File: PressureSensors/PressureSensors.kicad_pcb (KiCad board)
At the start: 2 copper layers, 40 x 40 mm, 32 parts, among them J1 Conn_02x03_Odd_Even, U1 LPS22HB, U2 LPS22HB, U3 LPS22HB, U4 LPS22HB, U5 PCA9548ADB, U6 K78xxJT-500R3

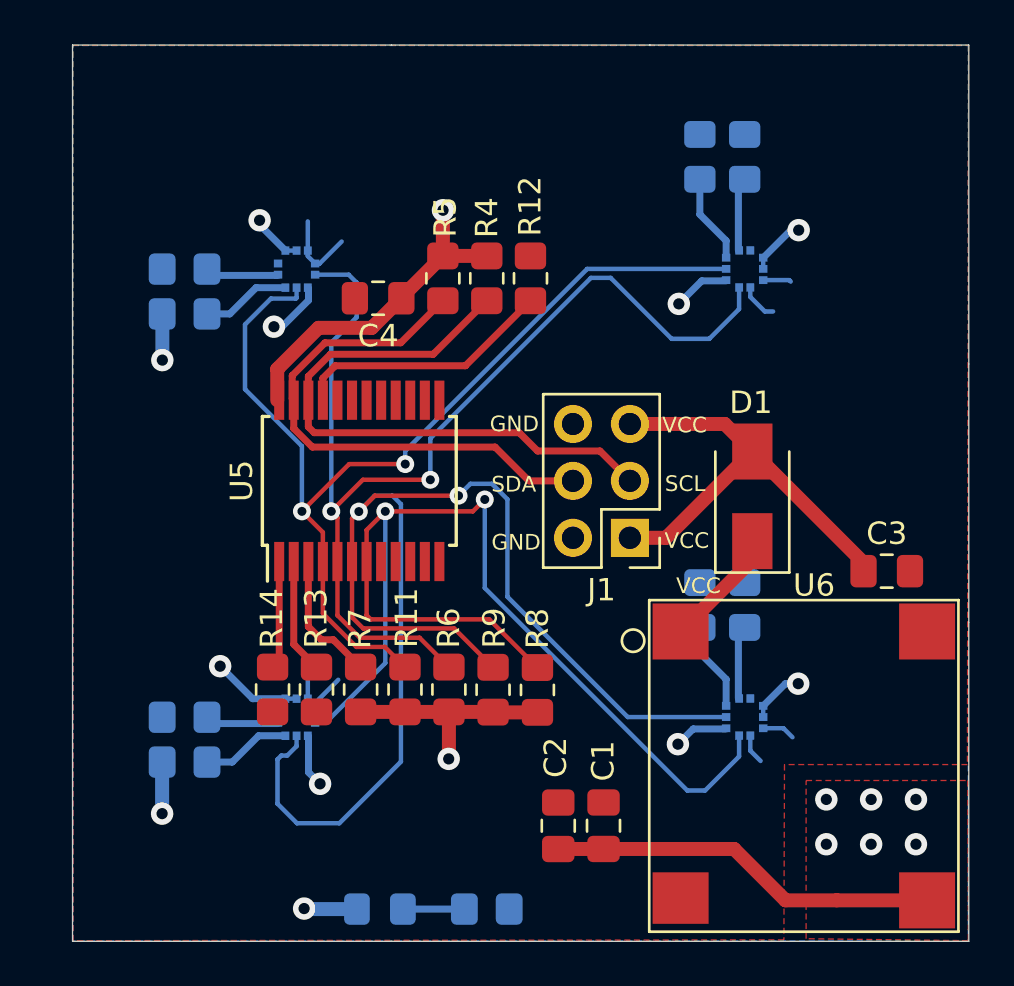
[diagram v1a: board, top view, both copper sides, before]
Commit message: Changed I2C multiplexer to 2 channel
Changed power source to LDO

Corrected spacing between sensors

Added missing capacitor for sensors

Eliminated unnecesary resistors for sensors
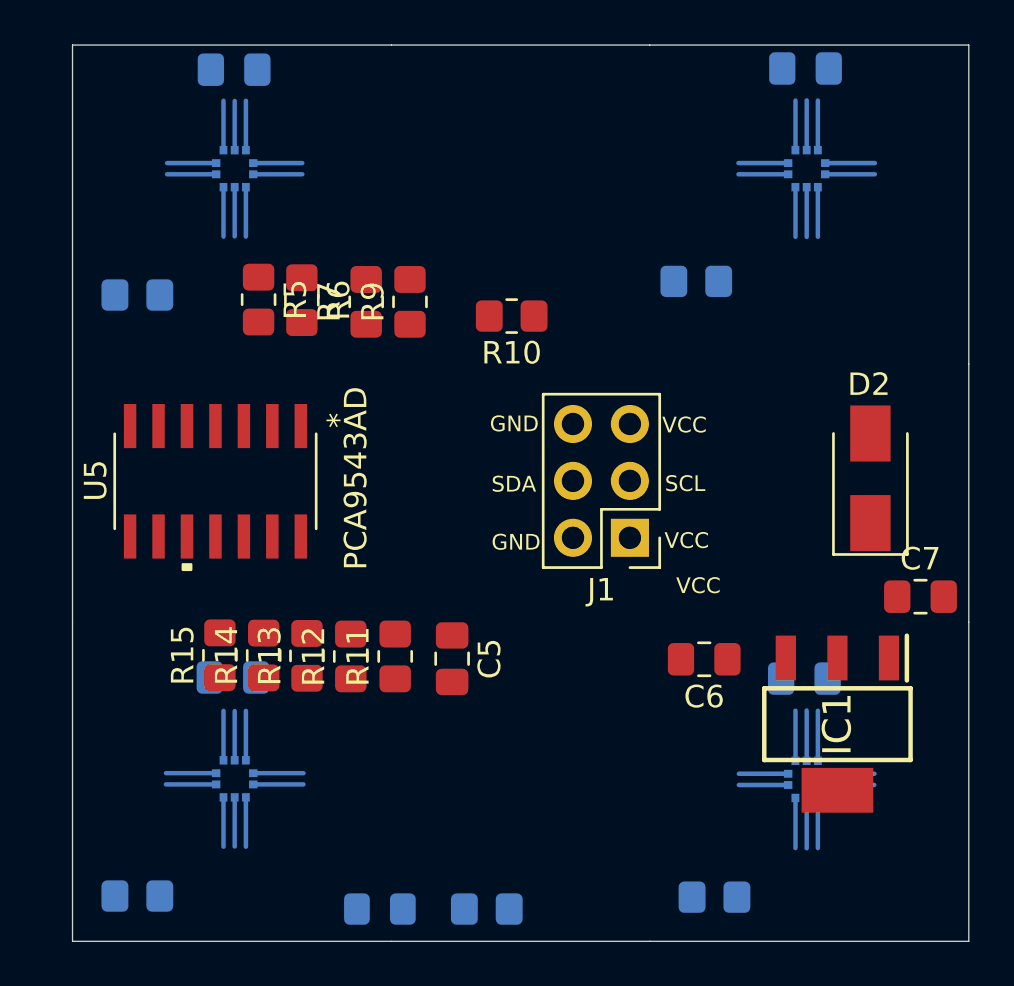
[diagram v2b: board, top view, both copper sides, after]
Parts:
- removed the R1 at (153.8, 62.8)
- removed R16, R17: 10k, Resistor_SMD:R_0805_2012Metric_Pad1.20x1.40mm_HandSolder
- removed the R4 at (142.3, 68.2)
- removed the R8 at (144.6, 86.6)
- removed U6: K78xxJT-500R3, Custom:K7803JT-500R3-SMD
- added C5: 1u, Capacitor_SMD:C_0805_2012Metric_Pad1.18x1.45mm_HandSolder, F.Cu at (140.8, 85.2)
- added C6: 4.7u, Capacitor_SMD:C_0805_2012Metric_Pad1.18x1.45mm_HandSolder, F.Cu at (152.0, 85.2)
- added C7: 0.1u, Capacitor_SMD:C_0805_2012Metric_Pad1.18x1.45mm_HandSolder, F.Cu at (161.7, 82.4)
- added IC1: BD733L2FP3-CE2, Custom:SOT230P700X180-4N, F.Cu at (158.0, 88.1)
- added R10: 10k, Resistor_SMD:R_0805_2012Metric_Pad1.20x1.40mm_HandSolder, F.Cu at (143.4, 69.9)
- C1, C2: value 22u -> 100n; moved to B.Cu
- C3: value 10u -> 100n; moved to B.Cu
- C4: value 1u -> 100n; moved to B.Cu
- R15: moved to F.Cu
- U5: value PCA9548ADB -> PCA9543AD; footprint Package_SO:SSOP-24_5.3x8.2mm_P0.65mm -> Custom:PCA9543AD
- moved C2 36.7 mm to (131.1, 58.9), turned to 180 degrees
- moved C1 35.0 mm to (156.6, 58.8), turned to 180 degrees
- moved R12 18.7 mm to (136.3, 85.1), turned to 90 degrees
- moved R6 18.6 mm to (134.1, 69.2), turned to -90 degrees
- moved C4 18.1 mm to (131.0, 86.0)
- moved R9 17.7 mm to (138.9, 69.2)
- moved R7 17.4 mm to (137.0, 69.2)
- moved R15 17.3 mm to (130.4, 85.0), turned to 90 degrees
- moved R2 13.1 mm to (152.5, 95.8), turned to 0 degrees
- moved R5 8.28 mm to (132.2, 69.1)
- moved U5 6.42 mm to (130.2, 77.2), turned to -90 degrees
- moved R4 6.34 mm to (126.7, 95.8)
- moved C3 6.04 mm to (156.5, 86.1), turned to 180 degrees
- moved R1 5.56 mm to (151.7, 68.3), turned to 0 degrees
- moved D2 5.33 mm to (159.5, 77.1)
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- renumbered D3 to D1, D1 to D2, R2 to R1, R18 to R2, R19 to R4, R10 to R8
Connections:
- C3 pad 1: +12V -> +3V3
- D2 pad 1: Net-(D1-Pad1) -> /VCC
- R11 pad 1: Net-(R11-Pad1) -> +3V3
- R11 pad 2: +3V3 -> /SCL
- R12 pad 1: GND -> +3V3
- R13 pad 1: GND -> +3V3
- R13 pad 2: Net-(R13-Pad2) -> /SCL1
- R14 pad 1: GND -> +3V3
- R14 pad 2: Net-(R14-Pad2) -> /SDA1
- R15 pad 2: /CS2 -> Net-(R15-Pad2)
- R5 pad 2: /SDA -> /SCL0
- R6 pad 2: /SCL1 -> /SDA0
- R7 pad 1: +3V3 -> Net-(R7-Pad1)
- R7 pad 2: /SDA1 -> +3V3
- R9 pad 1: +3V3 -> Net-(R9-Pad1)
- R9 pad 2: /SDA2 -> +3V3
- U1 pad 2: /SCL1 -> /SCL0
- U1 pad 4: /SDA1 -> /SDA0
- U1 pad 6: /CS1 -> +3V3
- U2 pad 2: /SCL1 -> /SCL0
- U2 pad 4: /SDA1 -> /SDA0
- U2 pad 6: /CS2 -> +3V3
- U3 pad 2: /SCL2 -> /SCL1
- U3 pad 4: /SDA2 -> /SDA1
- U3 pad 6: /CS3 -> +3V3
- U4 pad 2: /SCL2 -> /SCL1
- U4 pad 4: /SDA2 -> /SDA1
- U4 pad 6: /CS4 -> +3V3
- U5 pad 1: Net-(R14-Pad2) -> GND
- U5 pad 10: unconnected-(U5-Pad10) -> /SCL1
- U5 pad 11: unconnected-(U5-Pad11) -> Net-(R12-Pad2)
- U5 pad 12: GND -> /SCL
- U5 pad 13: unconnected-(U5-Pad13) -> /SDA
- U5 pad 14: unconnected-(U5-Pad14) -> +3V3
- U5 pad 2: Net-(R13-Pad2) -> GND
- U5 pad 3: Net-(R11-Pad1) -> Net-(R9-Pad1)
- U5 pad 4: /SDA1 -> Net-(R7-Pad1)
- U5 pad 5: /SCL1 -> /SDA0
- U5 pad 6: /SDA2 -> /SCL0
- U5 pad 7: /SCL2 -> GND
- U5 pad 8: unconnected-(U5-Pad8) -> Net-(R15-Pad2)
- U5 pad 9: unconnected-(U5-Pad9) -> /SDA1
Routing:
- net /SDA2: track 60.2 -> 0.00 mm, vias 2 -> 0
- net /SCL2: track 49.8 -> 0.00 mm, vias 2 -> 0
- net /SCL1: track 49.6 -> 4.43 mm, vias 2 -> 0
- net /SDA1: track 46.0 -> 4.44 mm, vias 2 -> 0
- net +3V3: track 55.5 -> 26.6 mm, vias 8 -> 0
- net /SCL: track 27.0 -> 0.00 mm
- net /SDA: track 23.9 -> 0.00 mm
- net +12V: track 20.4 -> 0.00 mm
- net Net-(R12-Pad2): track 11.7 -> 0.00 mm
- net Net-(R11-Pad1): track 5.99 -> 0.00 mm
- net Net-(D1-Pad1): track 5.36 -> 0.00 mm
- net Net-(R13-Pad2): track 5.13 -> 0.00 mm
- net Net-(R14-Pad2): track 4.83 -> 0.00 mm
- net /SDA0: track 0.00 -> 4.42 mm
- net /SCL0: track 0.00 -> 4.41 mm
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- removed copper zone on B.Cu, net +3V3
- removed copper zone on F.Cu, net +3V3
- removed copper zone on F.Cu, net GND

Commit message: Routed with new components
Deleted address selection resistors
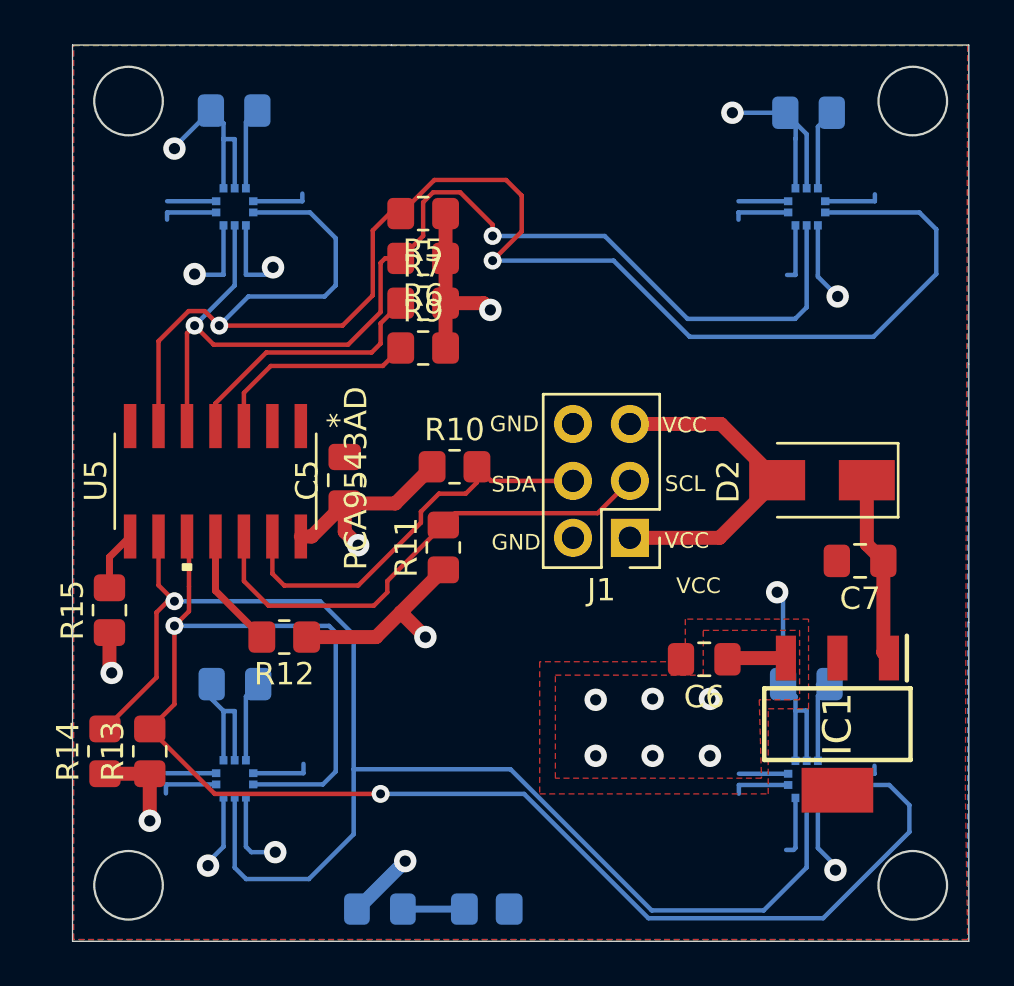
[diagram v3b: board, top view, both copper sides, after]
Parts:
- removed R1, R2, R3, R4: 10k, Resistor_SMD:R_0805_2012Metric_Pad1.20x1.40mm_HandSolder
- moved C5 9.30 mm to (136.0, 77.2), turned to 90 degrees
- moved R5 8.29 mm to (139.5, 65.3), turned to 180 degrees
- moved R14 8.28 mm to (125.3, 89.3)
- moved R13 8.21 mm to (127.3, 89.3)
- moved R10 7.19 mm to (140.9, 76.6), turned to 0 degrees
- moved R6 5.73 mm to (139.5, 67.3), turned to 180 degrees
- moved R15 5.32 mm to (125.5, 83.0)
- moved R11 5.32 mm to (140.4, 80.2)
- moved C7 3.13 mm to (159.0, 80.8), turned to 180 degrees
- moved R12 3.09 mm to (133.3, 84.2), turned to 180 degrees
- moved R7 2.54 mm to (139.5, 69.3), turned to 0 degrees
- moved D2 2.16 mm to (157.3, 77.2), turned to 180 degrees
- moved R9 2.14 mm to (139.5, 71.3), turned to 0 degrees
- moved C1 1.98 mm to (156.7, 60.8)
- moved C2 1.83 mm to (131.1, 60.7)
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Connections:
- U1 pad 5: /SA01 -> +3V3
- U2 pad 5: /SA02 -> GND
- U3 pad 5: /SA03 -> +3V3
- U4 pad 5: /SA04 -> GND
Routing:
- net /SCL1: track 4.43 -> 71.1 mm, vias 0 -> 2
- net /SCL0: track 4.41 -> 70.8 mm, vias 0 -> 2
- net /SDA1: track 4.44 -> 64.1 mm, vias 0 -> 1
- net +3V3: track 26.6 -> 75.8 mm, vias 0 -> 11
- net /SDA0: track 4.42 -> 49.0 mm, vias 0 -> 2
- net GND: track 26.6 -> 60.4 mm, vias 0 -> 10
- net /SCL: track 0.00 -> 22.3 mm
- net /SDA: track 0.00 -> 18.5 mm
- net +12V: track 0.00 -> 15.3 mm
- net Net-(R7-Pad1): track 0.00 -> 11.7 mm
- net Net-(R9-Pad1): track 0.00 -> 9.31 mm
- net /VCC: track 0.00 -> 8.35 mm
- net Net-(R12-Pad2): track 0.00 -> 5.35 mm
- net Net-(D1-Pad2): track 0.00 -> 2.75 mm
- net Net-(R15-Pad2): track 0.00 -> 2.67 mm
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- added copper zone on B.Cu, net +3V3
- added copper zone on F.Cu, net +3V3
- added copper zone on F.Cu, net GND
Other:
- outline, holes or cut-outs redrawn

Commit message: DRC check for v1.1 of pressure sensors board
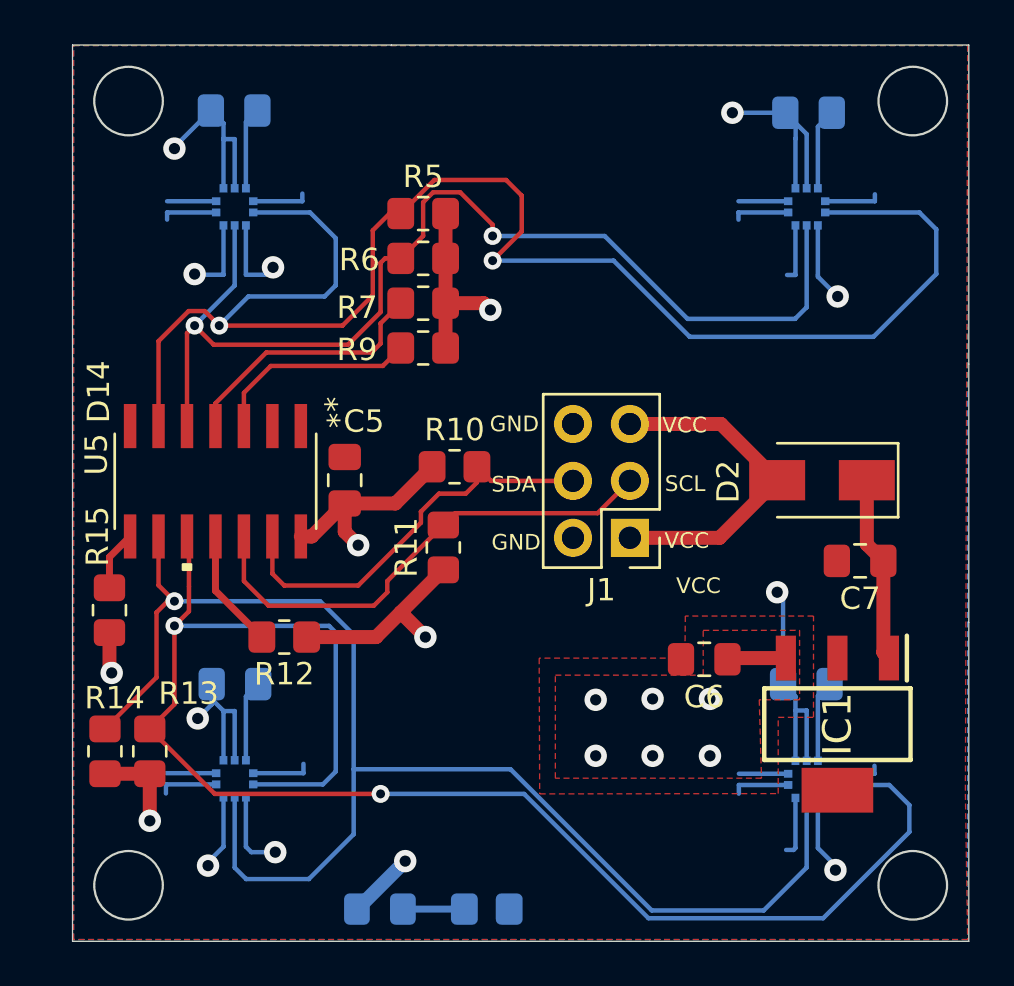
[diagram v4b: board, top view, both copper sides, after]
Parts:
- U5: value PCA9543AD -> D14
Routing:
- net GND: track 60.4 -> 62.2 mm, vias 10 -> 11
- net +3V3: track 75.8 -> 75.2 mm

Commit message: Flipped side of sensor capacitors
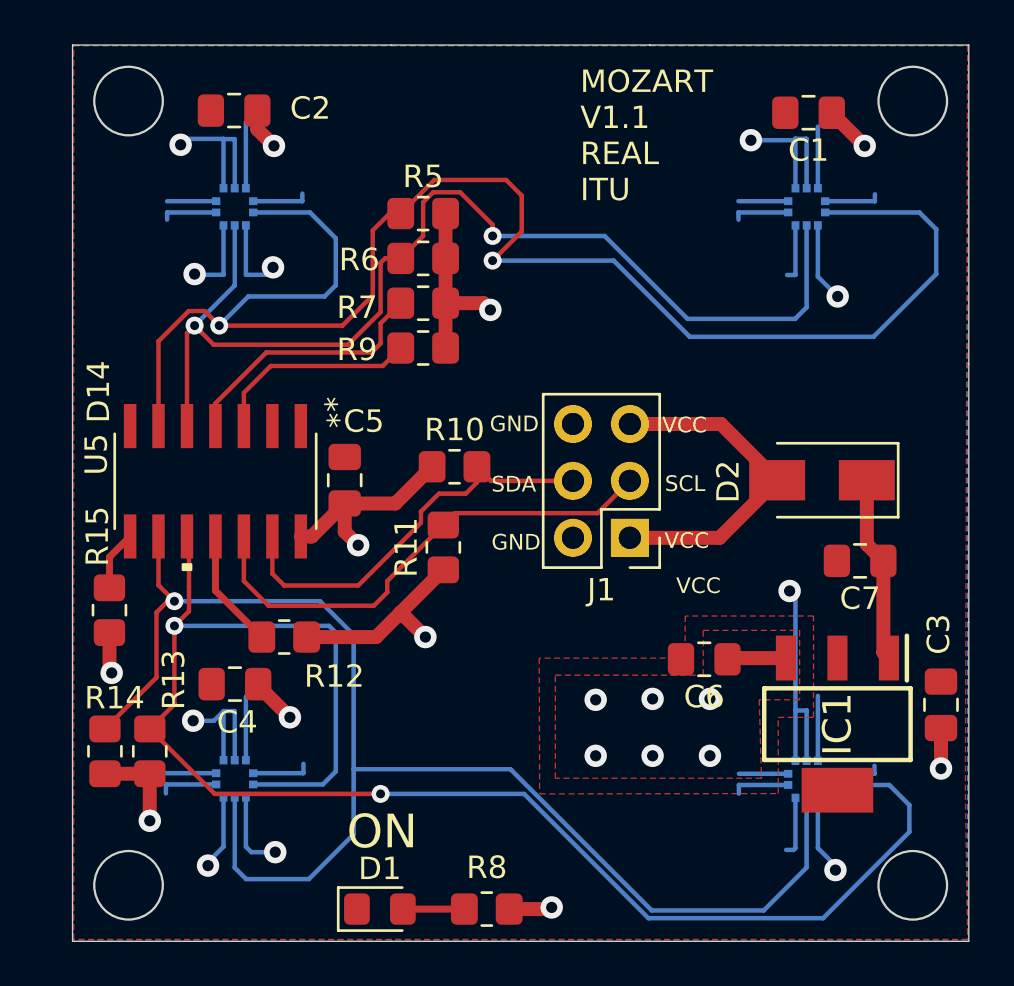
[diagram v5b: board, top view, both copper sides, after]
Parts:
- C1, C2, C3, C4, D1, R8: moved to F.Cu
- moved C3 6.08 mm to (162.6, 87.2), turned to 90 degrees
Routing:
- net GND: track 62.2 -> 51.8 mm, vias 11 -> 10
- net +3V3: track 75.2 -> 81.8 mm, vias 11 -> 16
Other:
- board text added: "MOZART V1.1 REAL ITU"
- board text removed: "MOZART V1.0 REAL ITU"

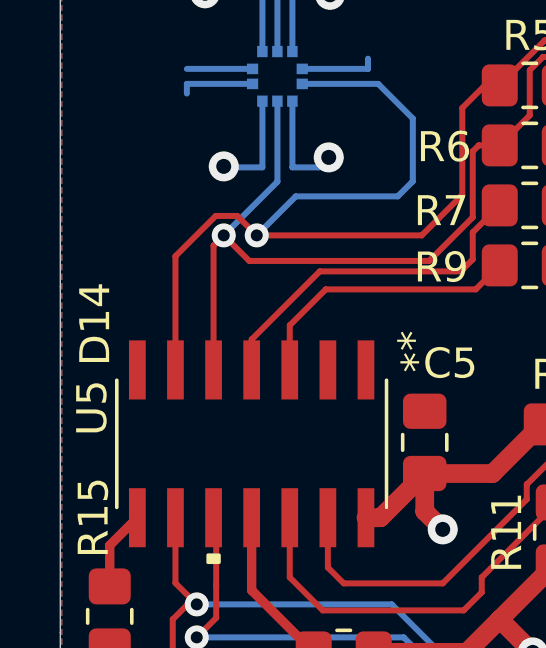
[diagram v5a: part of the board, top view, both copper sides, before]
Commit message: Changed power source capacitor from 0.1u to 1u
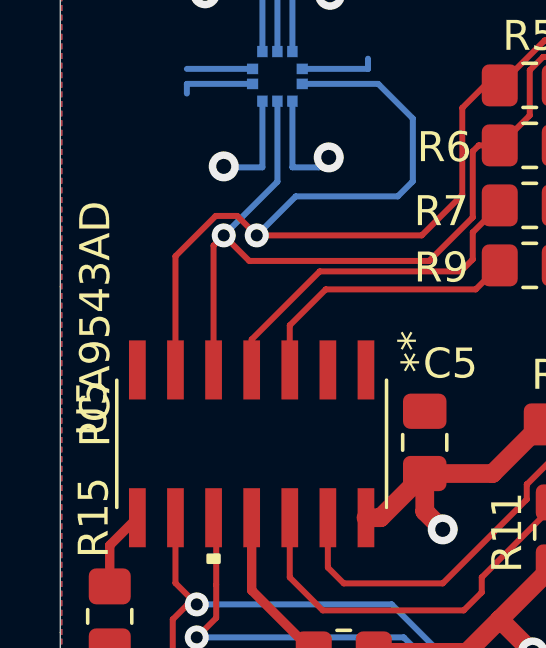
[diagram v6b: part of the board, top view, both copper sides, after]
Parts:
- C7: value 0.1u -> 1u
- U5: value D14 -> PCA9543AD
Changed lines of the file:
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@@
       (effects (font (size 1 1) (thickness 0.15)))
     )
-    (fp_text value "0.1u" (at 0 1.68) (layer "F.Fab")
+    (fp_text value "1u" (at 0 1.68) (layer "F.Fab")
       (effects (font (size 1 1) (thickness 0.15)))
     )
@@
       (effects (font (size 1 1) (thickness 0.15)))
     )
-    (fp_text value "D14" (at -3.99415 5.211684 -90) (layer "F.SilkS")
-      (effects (font (size 1 1) (thickness 0.15)))
-    )
+    (fp_text value "PCA9543AD" (at -3.99415 5.211684 -90) (layer "F.SilkS")
+      (effects (font (size 1 1) (thickness 0.15)))
+    )
